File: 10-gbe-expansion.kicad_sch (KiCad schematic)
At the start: 0 parts

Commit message: [#80813] Draft X710 power, PCIe and 10GbE interfaces
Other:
- added sheet X710-AT2 10GbE (x710-at2-10gbe.kicad_sch)
- added sheet X710-AT2 PCIe (x710-at2-pcie.kicad_sch)
- added sheet X710-AT2 power (x710-at2-power.kicad_sch)
- note added: "X710-AT2"

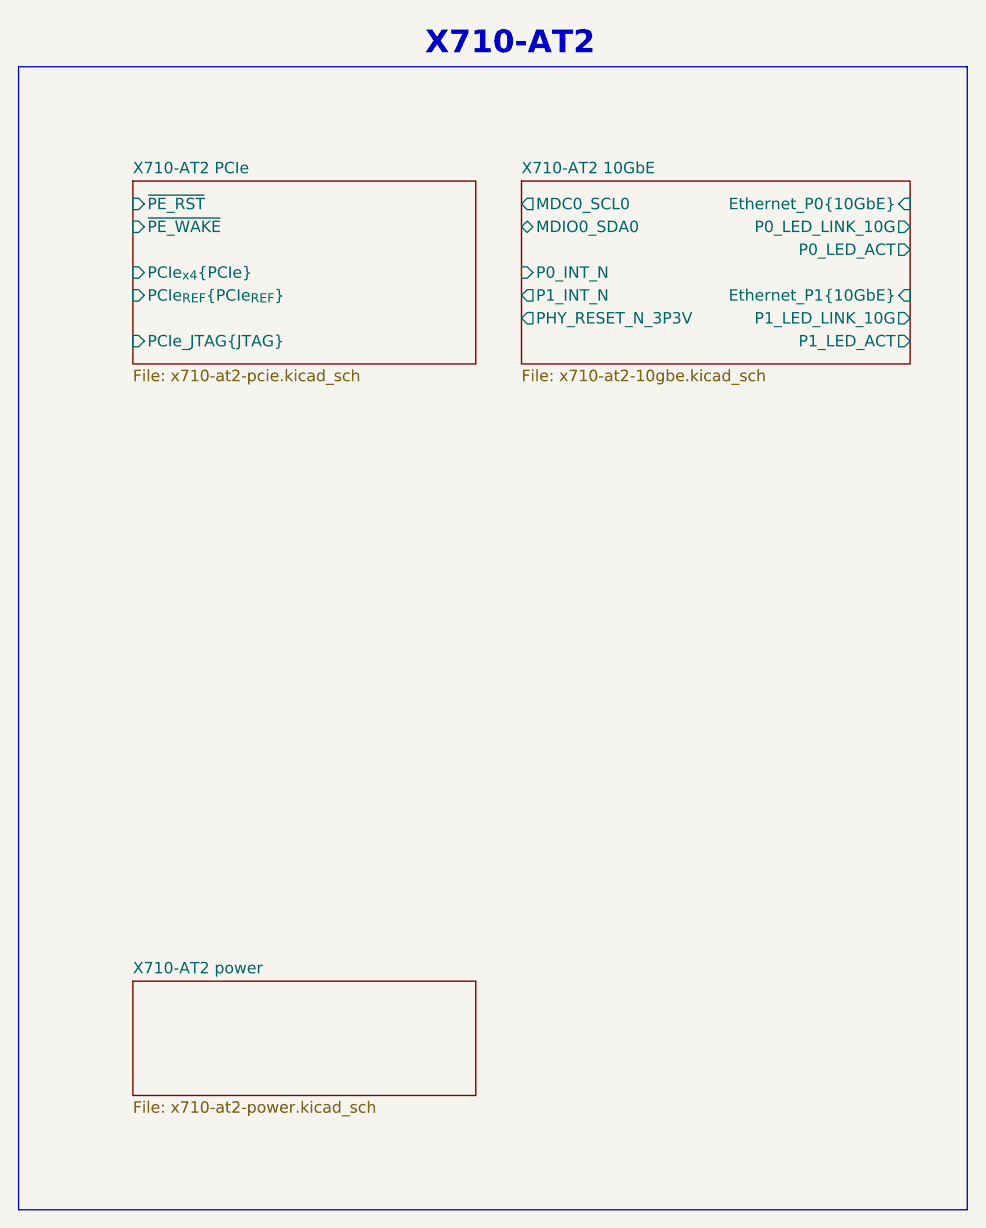
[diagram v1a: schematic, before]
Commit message: [#80813] Draft X710 RSVD and misc
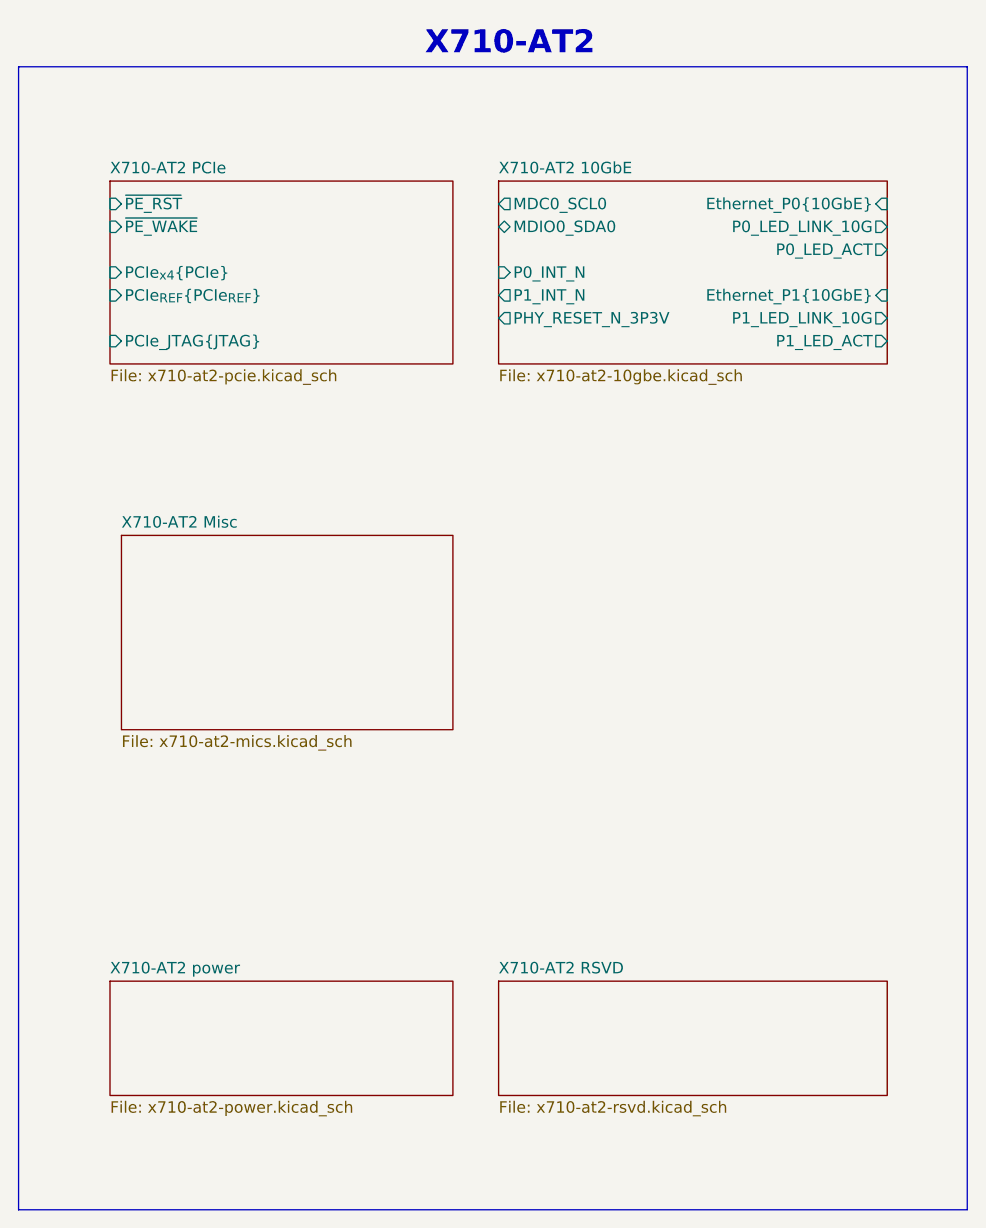
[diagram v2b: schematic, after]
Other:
- added sheet X710-AT2 Misc (x710-at2-mics.kicad_sch)
- added sheet X710-AT2 RSVD (x710-at2-rsvd.kicad_sch)
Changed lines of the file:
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@@
 	)
 	(sheet
-		(at 186.69 96.52)
+		(at 184.15 96.52)
 		(size 38.1 20.32)
 		(exclude_from_sim no)
@@
 		)
 		(property "Sheetname" "X710-AT2 PCIe"
-			(at 186.69 95.8084 0)
+			(at 184.15 95.8084 0)
 			(effects
 				(font
@@
 		)
 		(property "Sheetfile" "x710-at2-pcie.kicad_sch"
-			(at 186.69 117.4246 0)
+			(at 184.15 117.4246 0)
 			(effects
 				(font
@@
 		)
 		(pin "PCIe_JTAG{JTAG}" input
-			(at 186.69 114.3 180)
+			(at 184.15 114.3 180)
 			(effects
 				(font
@@
 		)
 		(pin "PCIe_{REF}{PCIe_{REF}}" input
-			(at 186.69 109.22 180)
+			(at 184.15 109.22 180)
 			(effects
 				(font
@@
 		)
 		(pin "PCIe_{x4}{PCIe}" input
-			(at 186.69 106.68 180)
+			(at 184.15 106.68 180)
 			(effects
 				(font
@@
 		)
 		(pin "~{PE_RST}" input
-			(at 186.69 99.06 180)
+			(at 184.15 99.06 180)
 			(effects
 				(font
@@
 		)
 		(pin "~{PE_WAKE}" input
-			(at 186.69 101.6 180)
+			(at 184.15 101.6 180)
 			(effects
 				(font
@@
 	)
 	(sheet
-		(at 229.87 96.52)
+		(at 227.33 96.52)
 		(size 43.18 20.32)
 		(exclude_from_sim no)
@@
 		)
 		(property "Sheetname" "X710-AT2 10GbE"
-			(at 229.87 95.8084 0)
+			(at 227.33 95.8084 0)
 			(effects
 				(font
@@
 		)
 		(property "Sheetfile" "x710-at2-10gbe.kicad_sch"
-			(at 229.87 117.4246 0)
+			(at 227.33 117.4246 0)
 			(effects
 				(font
@@
 		)
 		(pin "Ethernet_P0{10GbE}" input
-			(at 273.05 99.06 0)
+			(at 270.51 99.06 0)
 			(effects
 				(font
@@
 		)
 		(pin "Ethernet_P1{10GbE}" input
-			(at 273.05 109.22 0)
+			(at 270.51 109.22 0)
 			(effects
 				(font
@@
 		)
 		(pin "MDC0_SCL0" output
-			(at 229.87 99.06 180)
+			(at 227.33 99.06 180)
 			(effects
 				(font
@@
 		)
 		(pin "P0_LED_ACT" output
-			(at 273.05 104.14 0)
+			(at 270.51 104.14 0)
 			(effects
 				(font
@@
 		)
 		(pin "P0_LED_LINK_10G" output
-			(at 273.05 101.6 0)
+			(at 270.51 101.6 0)
 			(effects
 				(font
@@
 		)
 		(pin "P1_LED_ACT" output
-			(at 273.05 114.3 0)
+			(at 270.51 114.3 0)
 			(effects
 				(font
@@
 		)
 		(pin "P1_LED_LINK_10G" output
-			(at 273.05 111.76 0)
+			(at 270.51 111.76 0)
 			(effects
 				(font
@@
 		)
 		(pin "MDIO0_SDA0" bidirectional
-			(at 229.87 101.6 180)
+			(at 227.33 101.6 180)
 			(effects
 				(font
@@
 		)
 		(pin "P0_INT_N" input
-			(at 229.87 106.68 180)
+			(at 227.33 106.68 180)
 			(effects
 				(font
@@
 		)
 		(pin "P1_INT_N" output
-			(at 229.87 109.22 180)
+			(at 227.33 109.22 180)
 			(effects
 				(font
@@
 		)
 		(pin "PHY_RESET_N_3P3V" output
-			(at 229.87 111.76 180)
+			(at 227.33 111.76 180)
 			(effects
 				(font
@@
 	)
 	(sheet
-		(at 186.69 185.42)
+		(at 227.33 185.42)
+		(size 43.18 12.7)
+		(exclude_from_sim no)
+		(in_bom yes)
+		(on_board yes)
+		(dnp no)
+		(fields_autoplaced yes)
+		(stroke
+			(width 0.1524)
+			(type solid)
+		)
+		(fill
+			(color 255 255 194 1.0000)
+		)
+		(property "Sheetname" "X710-AT2 RSVD"
+			(at 227.33 184.7084 0)
+			(effects
+				(font
+					(size 1.27 1.27)
+				)
+				(justify left bottom)
+			)
+		)
+		(property "Sheetfile" "x710-at2-rsvd.kicad_sch"
+			(at 227.33 198.7046 0)
+			(effects
+				(font
+					(size 1.27 1.27)
+				)
+				(justify left top)
+			)
+		)
+		(instances
+			(project "10-gbe-expansion"
+				(path "/04bda987-e5eb-48b4-9e90-d8211dc11b39"
+					(page "5")
+				)
+			)
+		)
+	)
+	(sheet
+		(at 184.15 185.42)
 		(size 38.1 12.7)
 		(exclude_from_sim no)
@@
 		)
 		(property "Sheetname" "X710-AT2 power"
-			(at 186.69 184.7084 0)
+			(at 184.15 184.7084 0)
 			(effects
 				(font
@@
 		)
 		(property "Sheetfile" "x710-at2-power.kicad_sch"
-			(at 186.69 198.7046 0)
+			(at 184.15 198.7046 0)
 			(effects
 				(font
@@
 				)
 			)
+		)
+	)
+	(sheet
+		(at 185.42 135.89)
+		(size 36.83 21.59)
+		(exclude_from_sim no)
+		(in_bom yes)
+		(on_board yes)
+		(dnp no)
+		(fields_autoplaced yes)
+		(stroke
+			(width 0.1524)
+			(type solid)
+		)
+		(fill
+			(color 255 255 194 1.0000)
+		)
+		(property "Sheetname" "X710-AT2 Misc"
+			(at 185.42 135.1784 0)
+			(effects
+				(font
+					(size 1.27 1.27)
+				)
+				(justify left bottom)
+			)
+		)
+		(property "Sheetfile" "x710-at2-mics.kicad_sch"
+			(at 185.42 158.0646 0)
+			(effects
+				(font
+					(size 1.27 1.27)
+				)
+				(justify left top)
+			)
+		)
+		(instances
+			(project "10-gbe-expansion"
+				(path "/04bda987-e5eb-48b4-9e90-d8211dc11b39"
+					(page "6")
+				)
+			)

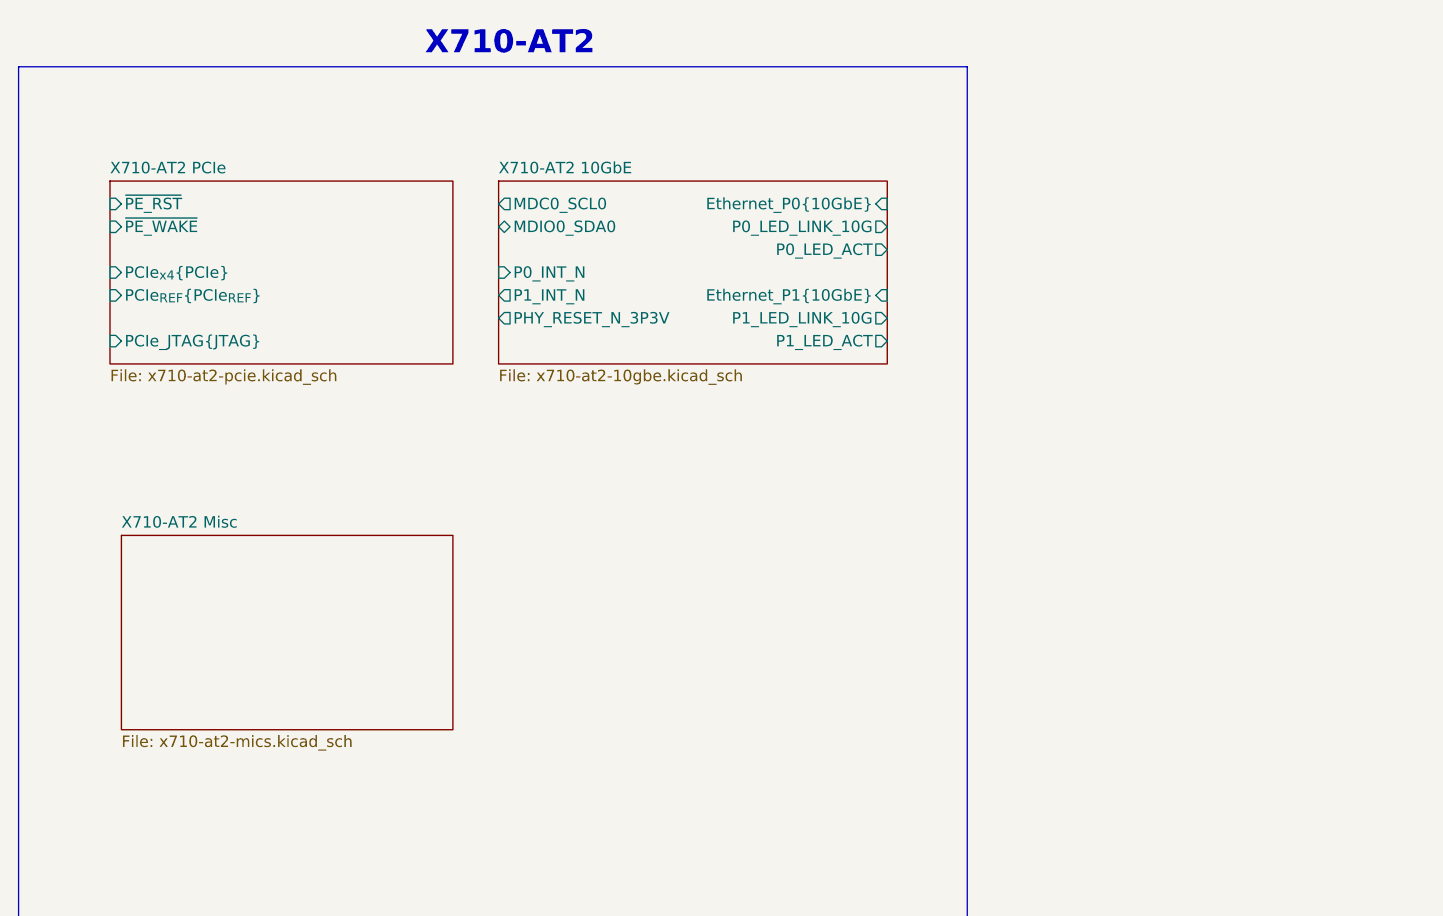
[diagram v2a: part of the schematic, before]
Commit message: [#80813] Add RJ45 connectors, add SMBus, FLASH SPI and misc
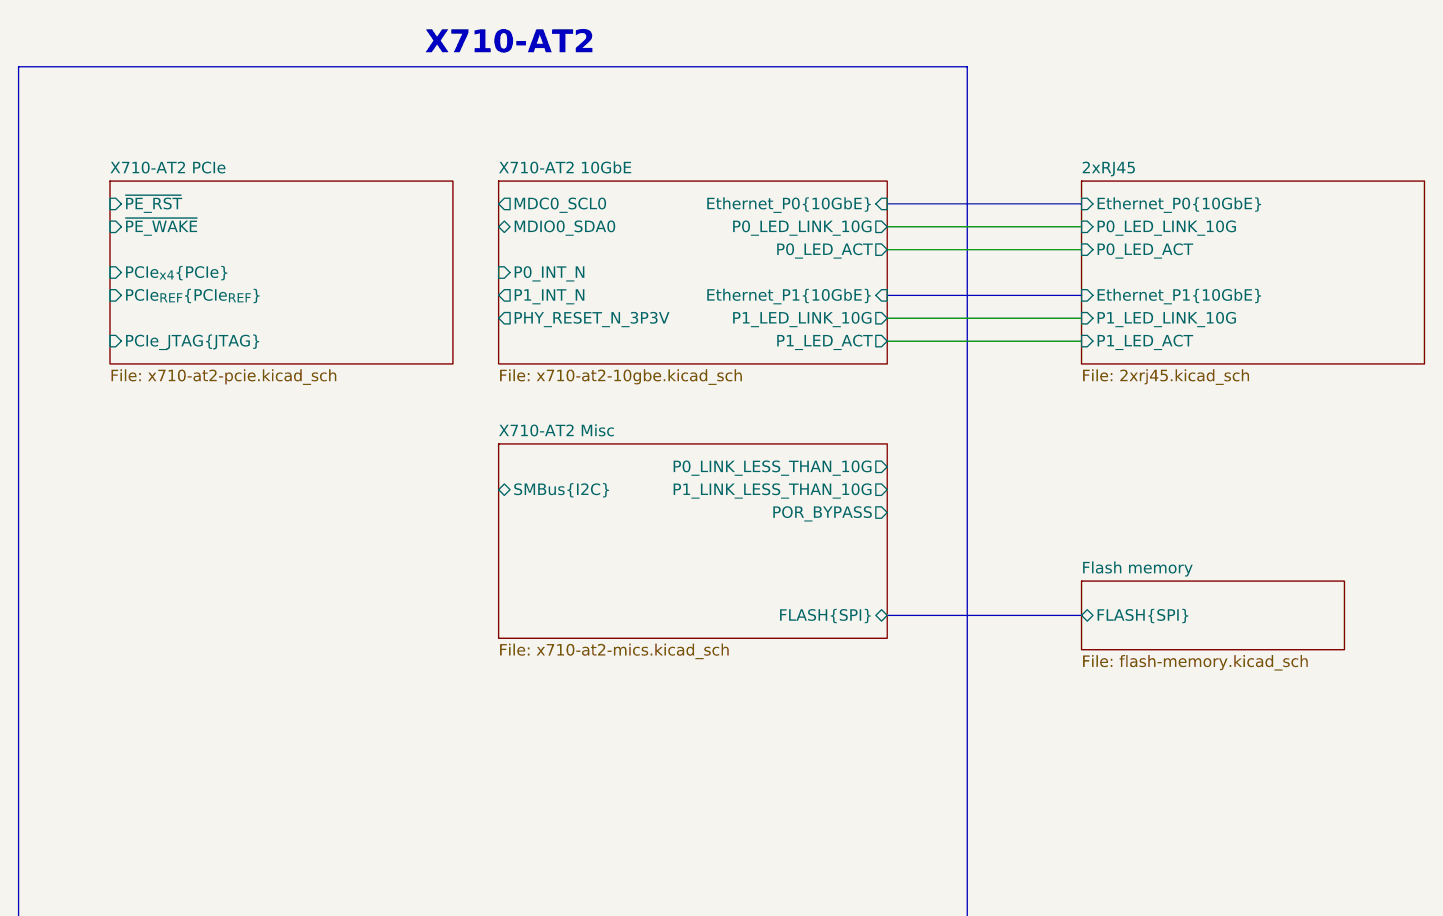
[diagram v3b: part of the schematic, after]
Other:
- added sheet 2xRJ45 (2xrj45.kicad_sch)
- added sheet Flash memory (flash-memory.kicad_sch)
- sheet X710-AT2 Misc ports: added FLASH{SPI}, P0_LINK_LESS_THAN_10G, P1_LINK_LESS_THAN_10G, POR_BYPASS, SMBus{I2C}; removed none

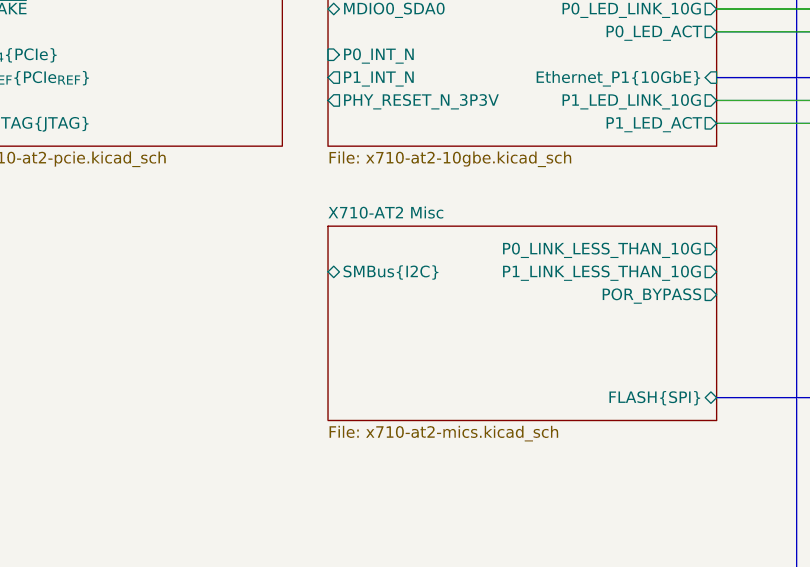
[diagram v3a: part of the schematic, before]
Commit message: [#80813] Add NCSI bus
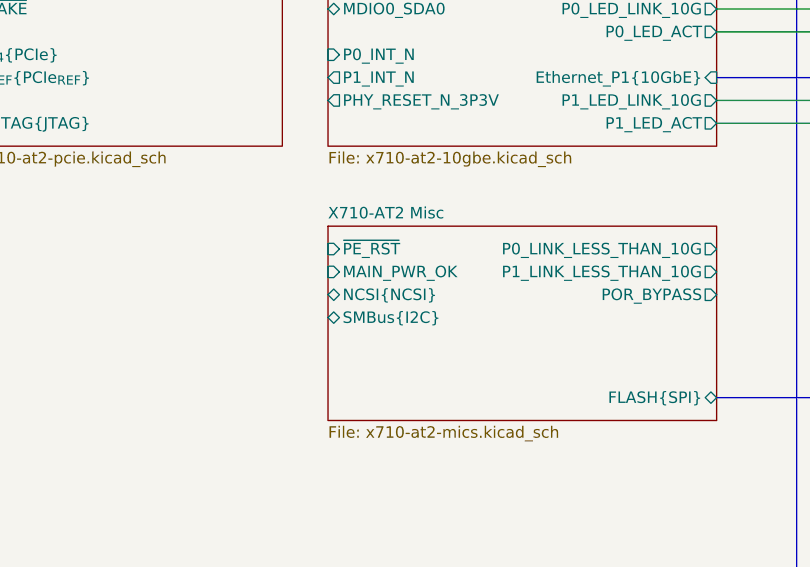
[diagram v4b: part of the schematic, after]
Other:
- sheet X710-AT2 Misc ports: added MAIN_PWR_OK, NCSI{NCSI}, ~{PE_RST}; removed none
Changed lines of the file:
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@@
 		)
 		(pin "SMBus{I2C}" bidirectional
-			(at 227.33 130.81 180)
+			(at 227.33 135.89 180)
 			(effects
 				(font
@@
 			)
 		)
+		(pin "MAIN_PWR_OK" input
+			(at 227.33 130.81 180)
+			(effects
+				(font
+					(size 1.27 1.27)
+				)
+				(justify left)
+			)
+		)
+		(pin "NCSI{NCSI}" bidirectional
+			(at 227.33 133.35 180)
+			(effects
+				(font
+					(size 1.27 1.27)
+				)
+				(justify left)
+			)
+		)
+		(pin "~{PE_RST}" input
+			(at 227.33 128.27 180)
+			(effects
+				(font
+					(size 1.27 1.27)
+				)
+				(justify left)
+			)
+		)
